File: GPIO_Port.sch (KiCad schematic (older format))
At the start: 73 parts, among them J6 Conn_02x20_Odd_Even

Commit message: Reroute ribbon connector protection circuitry, switch to single ribbon cable configuration.
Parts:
- added D2, D3, D4, D5: BAT54S, Package_TO_SOT_SMD:SOT-323_SC-70, symbol Diode:BAT54S
- added R1, R2, R3, R4: 50, Resistor_SMD:R_0603_1608Metric, symbol Device:R
- D1, D10, D11, D12, D13, D14, D15, D16, D17, D18, D19, D2, D20, D21, D22, D23, D24, D25, D26, D27, D28, D29, D3, D30, D31, D32, D33, D34, D35, D36, D4, D5, D6, D7, D8, D9: footprint Package_TO_SOT_SMD:SOT-23 -> Package_TO_SOT_SMD:SOT-323_SC-70
- R1, R10, R11, R12, R13, R14, R15, R16, R17, R18, R19, R2, R20, R21, R22, R23, R24, R25, R26, R27, R28, R29, R3, R30, R31, R32, R33, R34, R35, R36, R4, R5, R6, R7, R8, R9: footprint Resistor_SMD:R_0805_2012Metric -> Resistor_SMD:R_0603_1608Metric
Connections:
- net +5V is gone; now on net P11: J6.11 (Pin_11)
- net GP0 is gone; now on net GP1: R1.2
- net +3V3: now also D2.2, D3.2, D4.2, D5.2; no longer J6.29 (Pin_29)
- net GND: now also D2.1, D3.1, D4.1, D5.1; no longer J6.12 (Pin_12), J6.30 (Pin_30)
- net GP1: no longer R2.1
- net GP10: now also R10.1; no longer R11.2
- net GP11: now also R1.2; no longer R12.1
- net GP12: now also R3.1; no longer R13.2
- net GP13: now also R11.2; no longer R14.1
- net GP14: now also R12.1; no longer R15.2
- net GP15: now also R13.2; no longer R16.1
- net GP16: now also R14.1; no longer R17.2
- net GP17: now also R15.2; no longer R18.1
- net GP18: now also R16.1; no longer R19.2
- net GP19: now also R17.2; no longer R20.1
- net GP2: now also R2.1; no longer R3.2
- net GP20: now also R18.1; no longer R21.2
- net GP21: now also R19.2; no longer R22.1
- net GP22: now also R20.1; no longer R23.2
- net GP23: now also R21.2; no longer R24.1
- net GP24: now also R22.1; no longer R25.2
- net GP25: now also R23.2; no longer R26.1
- net GP26: now also R24.1; no longer R27.2
- net GP27: now also R25.2; no longer R28.1
- net GP28: now also R26.1; no longer R29.2
- net GP29: now also R2.2; no longer R30.1
- net GP3: now also R3.2; no longer R4.1
- net GP30: now also R4.1; no longer R31.2
- net GP31: now also R27.2; no longer R32.1
- net GP32: now also R28.1; no longer R33.2
- net GP33: now also R29.2; no longer R34.1
- net GP34: now also R30.1; no longer R35.2
- net GP35: now also R31.2; no longer R36.1
- net GP4: now also R4.1; no longer R5.2
- net GP5: now also R5.2; no longer R6.1
- net GP6: now also R6.1; no longer R7.2
- net GP7: now also R7.2; no longer R8.1
- net GP8: now also R8.1; no longer R9.2
- net GP9: now also R9.2; no longer R10.1
- net P1: now also J6.1 (Pin_1), R1.1; no longer J6.2 (Pin_2), R2.2
- net P10: now also J6.10 (Pin_10), R10.2; no longer J6.13 (Pin_13), R11.1
- net P11: now also R1.1; no longer J6.14 (Pin_14), R12.2
- net P12: now also J6.12 (Pin_12), R3.2; no longer J6.15 (Pin_15), R13.1
- net P13: now also J6.13 (Pin_13), R11.1; no longer J6.16 (Pin_16), R14.2
- net P14: now also J6.14 (Pin_14), R12.2; no longer J6.17 (Pin_17), R15.1
- net P15: now also J6.15 (Pin_15), R13.1; no longer J6.18 (Pin_18), R16.2
- net P16: now also J6.16 (Pin_16), R14.2; no longer J6.19 (Pin_19), R17.1
- net P17: now also J6.17 (Pin_17), R15.1; no longer J6.20 (Pin_20), R18.2
- net P18: now also J6.18 (Pin_18), R16.2; no longer J6.21 (Pin_21), R19.1
- net P19: now also J6.19 (Pin_19), R17.1; no longer J6.22 (Pin_22), R20.2
- net P2: now also J6.2 (Pin_2), R2.2; no longer J6.3 (Pin_3), R3.1
- net P20: now also J6.20 (Pin_20), R18.2; no longer J6.23 (Pin_23), R21.1
- net P21: now also J6.21 (Pin_21), R19.1; no longer J6.24 (Pin_24), R22.2
- net P22: now also J6.22 (Pin_22), R20.2; no longer J6.25 (Pin_25), R23.1
- net P23: now also J6.23 (Pin_23), R21.1; no longer J6.26 (Pin_26), R24.2
- net P24: now also J6.24 (Pin_24), R22.2; no longer J6.27 (Pin_27), R25.1
- net P25: now also J6.25 (Pin_25), R23.1; no longer J6.28 (Pin_28), R26.2
- net P26: now also J6.26 (Pin_26), R24.2; no longer J6.31 (Pin_31), R27.1
- net P27: now also J6.27 (Pin_27), R25.1; no longer J6.32 (Pin_32), R28.2
- net P28: now also J6.28 (Pin_28), R26.2; no longer J6.33 (Pin_33), R29.1
- net P29: now also J6.29 (Pin_29), R2.1; no longer J6.34 (Pin_34), R30.2
- net P3: now also J6.3 (Pin_3), R3.1; no longer J6.4 (Pin_4), R4.2
- net P30: now also J6.30 (Pin_30), R4.2; no longer J6.35 (Pin_35), R31.1
- net P31: now also J6.31 (Pin_31), R27.1; no longer J6.36 (Pin_36), R32.2
- net P32: now also J6.32 (Pin_32), R28.2; no longer J6.37 (Pin_37), R33.1
- net P33: now also J6.33 (Pin_33), R29.1; no longer J6.38 (Pin_38), R34.2
- net P34: now also J6.34 (Pin_34), R30.2; no longer J6.39 (Pin_39), R35.1
- net P35: now also J6.35 (Pin_35), R31.1; no longer J6.40 (Pin_40), R36.2
- net P4: now also J6.4 (Pin_4), R4.2; no longer J6.5 (Pin_5), R5.1
- net P5: now also J6.5 (Pin_5), R5.1; no longer J6.6 (Pin_6), R6.2
- net P6: now also J6.6 (Pin_6), R6.2; no longer J6.7 (Pin_7), R7.1
- net P7: now also J6.7 (Pin_7), R7.1; no longer J6.8 (Pin_8), R8.2
- net P8: now also J6.8 (Pin_8), R8.2; no longer J6.9 (Pin_9), R9.1
- net P9: now also J6.9 (Pin_9), R9.1; no longer J6.10 (Pin_10), R10.2
- removed net P0: D1.3, J6.1 (Pin_1), R1.1
- new net GP36: R32.1
- new net GP37: R33.2
- new net GP38: R34.1
- new net GP39: R35.2
- new net GP40: R36.1
- new net P36: D1.3, J6.36 (Pin_36), R32.2
- new net P37: D2.3, J6.37 (Pin_37), R33.1
- new net P38: D3.3, J6.38 (Pin_38), R34.2
- new net P39: D4.3, J6.39 (Pin_39), R35.1
- new net P40: D5.3, J6.40 (Pin_40), R36.2

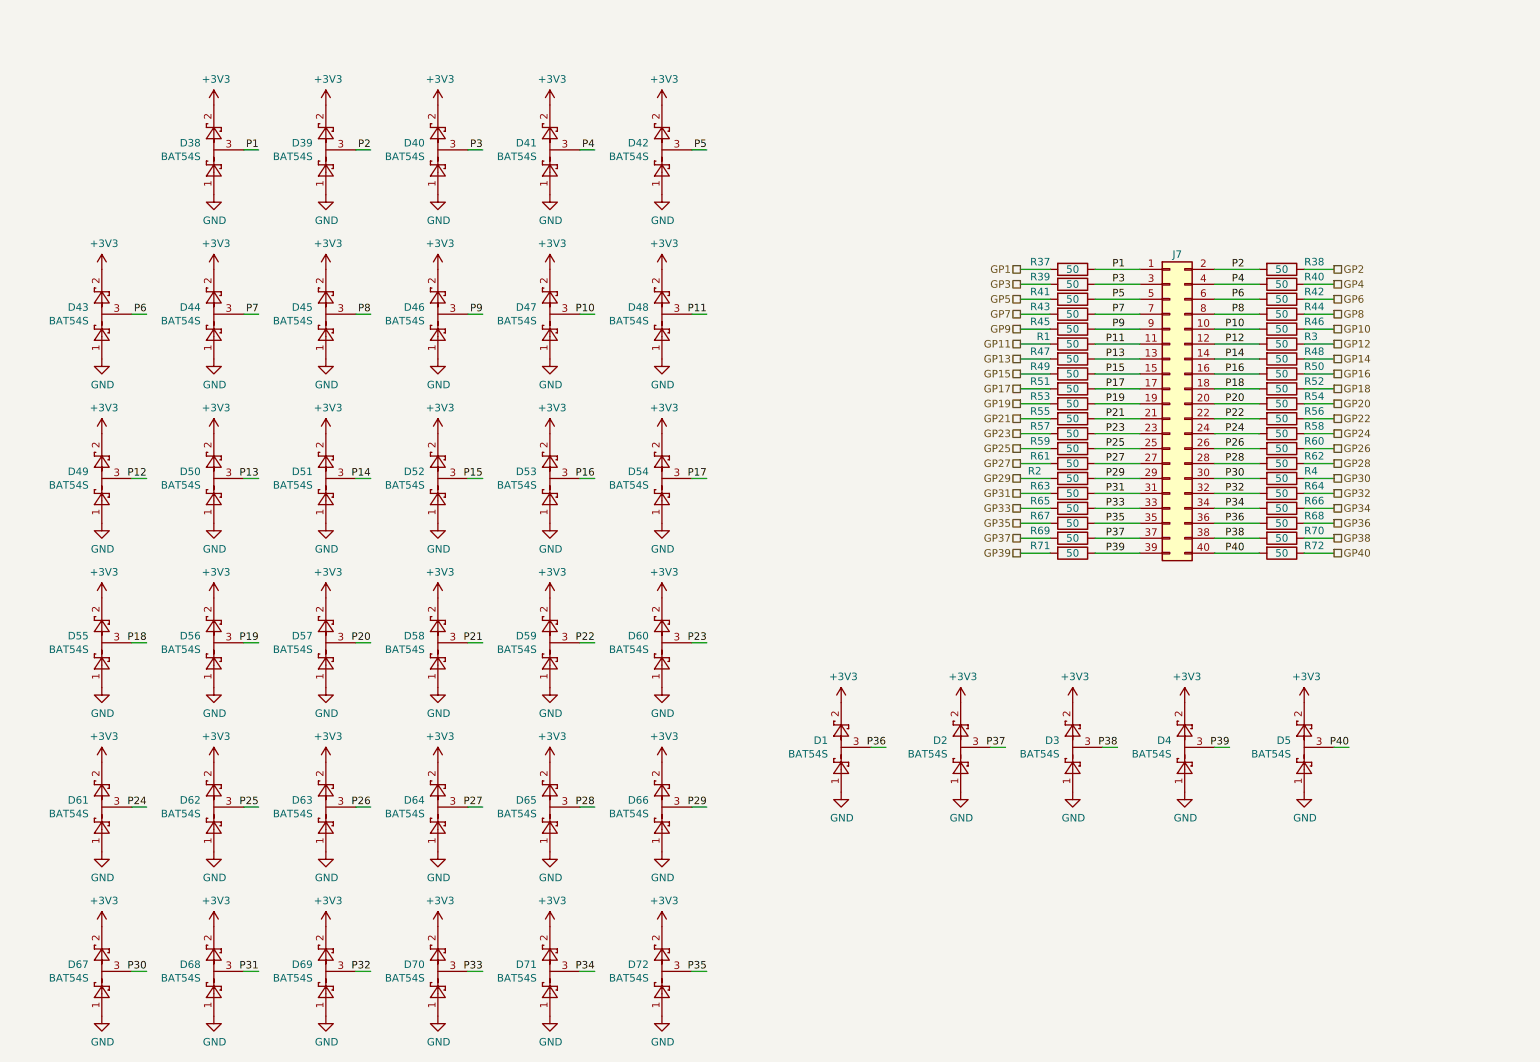
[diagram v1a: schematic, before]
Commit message: Change pin/bus labels in schematic
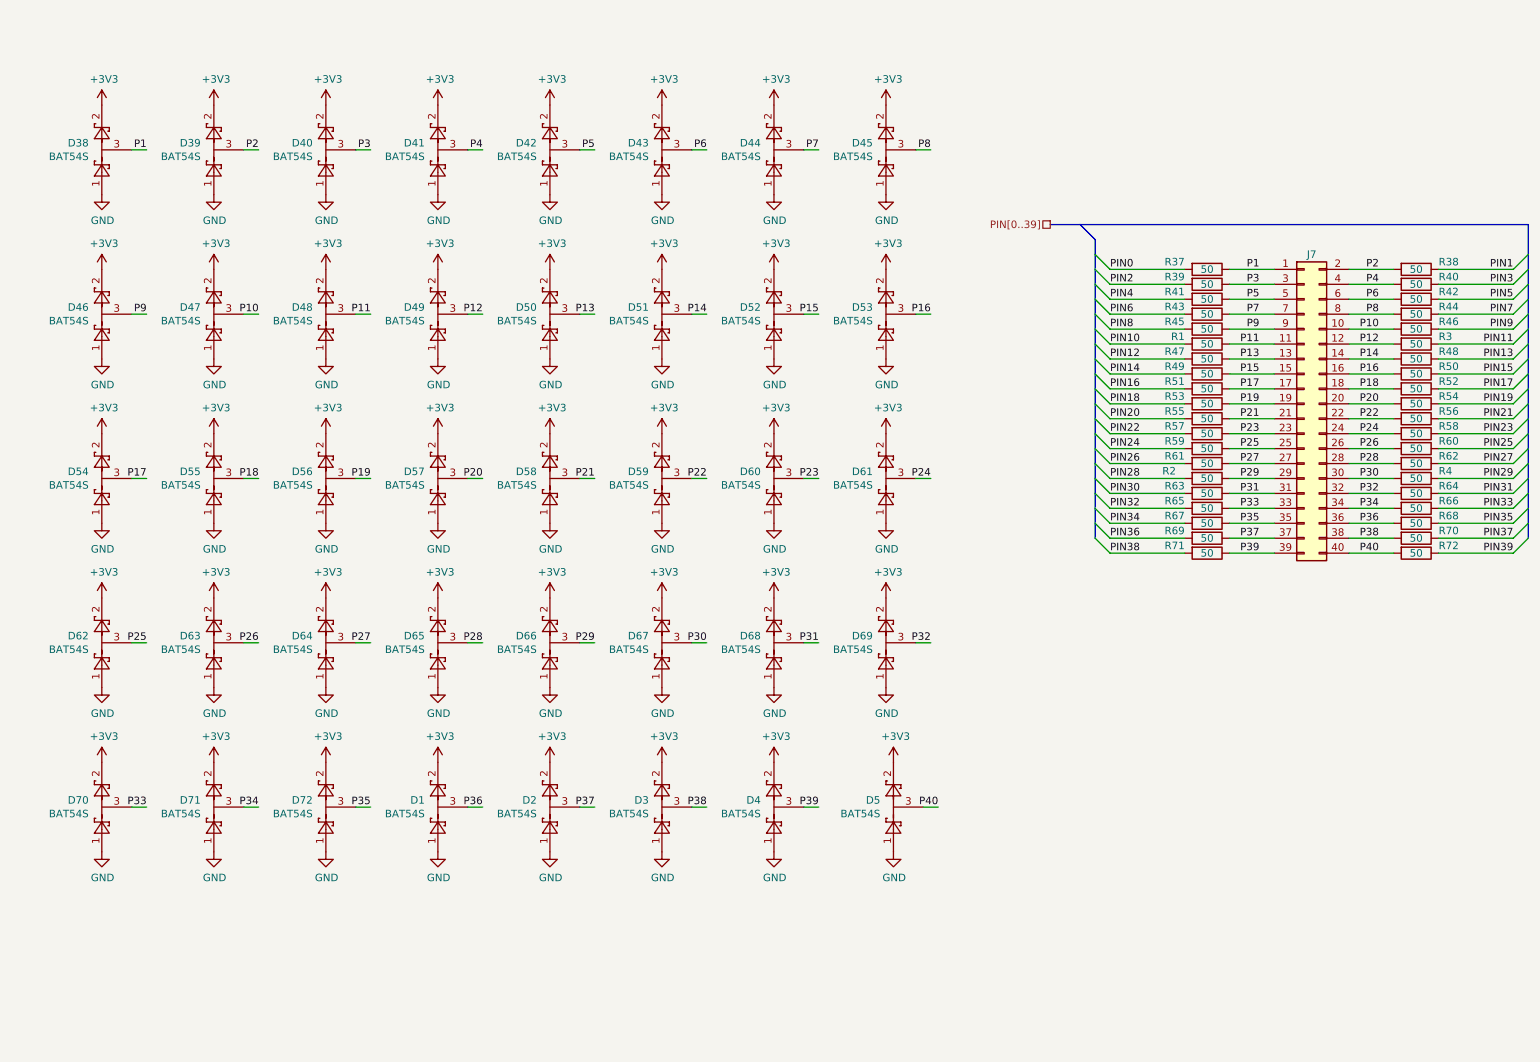
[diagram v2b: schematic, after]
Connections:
- net GP1 renamed PIN0
- net GP10 renamed PIN9
- net GP11 renamed PIN10
- net GP12 renamed PIN11
- net GP13 renamed PIN12
- net GP14 renamed PIN13
- net GP15 renamed PIN14
- net GP16 renamed PIN15
- net GP17 renamed PIN16
- net GP18 renamed PIN17
- net GP19 renamed PIN18
- net GP2 renamed PIN1
- net GP20 renamed PIN19
- net GP21 renamed PIN20
- net GP22 renamed PIN21
- net GP23 renamed PIN22
- net GP24 renamed PIN23
- net GP25 renamed PIN24
- net GP26 renamed PIN25
- net GP27 renamed PIN26
- net GP28 renamed PIN27
- net GP29 renamed PIN28
- net GP3 renamed PIN2
- net GP30 renamed PIN29
- net GP31 renamed PIN30
- net GP32 renamed PIN31
- net GP33 renamed PIN32
- net GP34 renamed PIN33
- net GP35 renamed PIN34
- net GP36 renamed PIN35
- net GP37 renamed PIN36
- net GP38 renamed PIN37
- net GP39 renamed PIN38
- net GP4 renamed PIN3
- net GP40 renamed PIN39
- net GP5 renamed PIN4
- net GP6 renamed PIN5
- net GP7 renamed PIN6
- net GP8 renamed PIN7
- net GP9 renamed PIN8
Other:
- moved on the sheet: D1, D2, D3, D38, D39, D4, D40, D41, D42, D43, D44, D45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

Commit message: Begin routing ribbon cable connector
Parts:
- renumbered D2 to D1, D11 to D10, D12 to D11, D13 to D12, D14 to D13, D15 to D14, D16 to D15, D17 to D16, D18 to D17, D19 to D18, D20 to D19, D3 to D2, D21 to D20, D22 to D21, D23 to D22, D24 to D23, D25 to D24, D26 to D25, D27 to D26, D28 to D27, D29 to D28, D30 to D29, D4 to D3, D31 to D30, D32 to D31, D33 to D32, D34 to D33, D35 to D34, D36 to D35, D1 to D36, D2 to D37, D3 to D38, D4 to D39, D5 to D4, D5 to D40, D6 to D5, D7 to D6, D8 to D7, D9 to D8, D10 to D9, J6 to J5, R1 to R11, R3 to R12, R11 to R13, R12 to R14, R13 to R15, R14 to R16, R15 to R17, R16 to R18, R17 to R19, R18 to R20, R19 to R21, R20 to R22, R21 to R23, R22 to R24, R23 to R25, R24 to R26, R25 to R27, R26 to R28, R2 to R29, R4 to R30, R27 to R31, R28 to R32, R29 to R33, R30 to R34, R31 to R35, R32 to R36, R33 to R37, R34 to R38, R35 to R39, R36 to R40

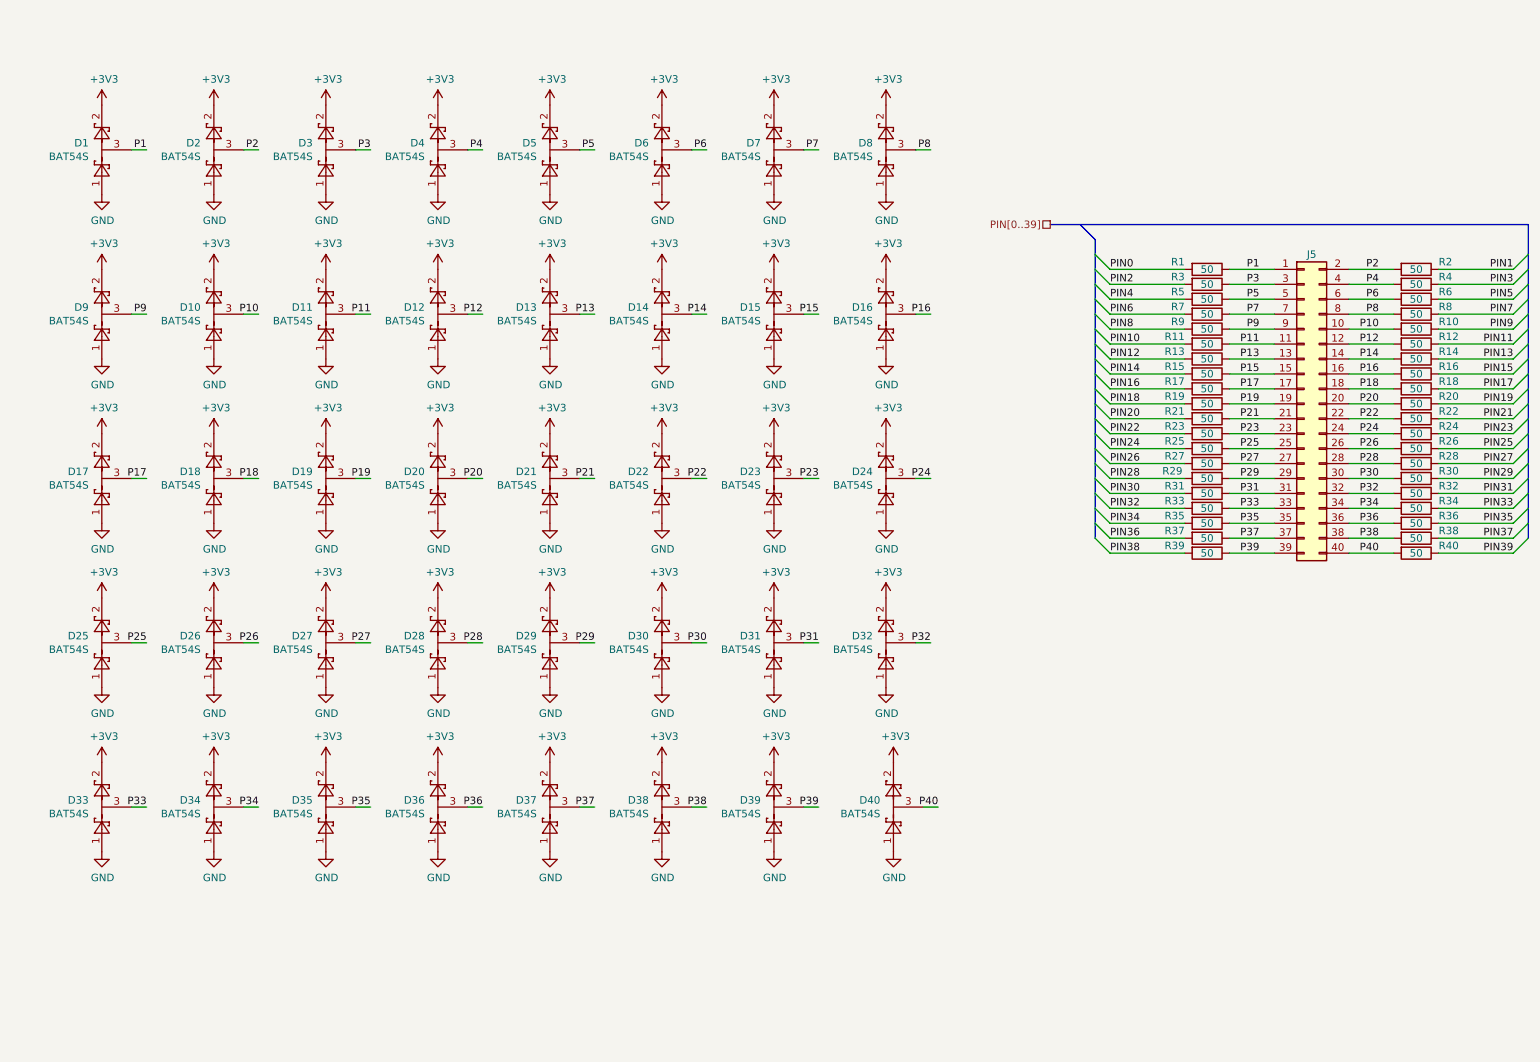
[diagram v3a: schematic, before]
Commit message: Finish routing GPIO port
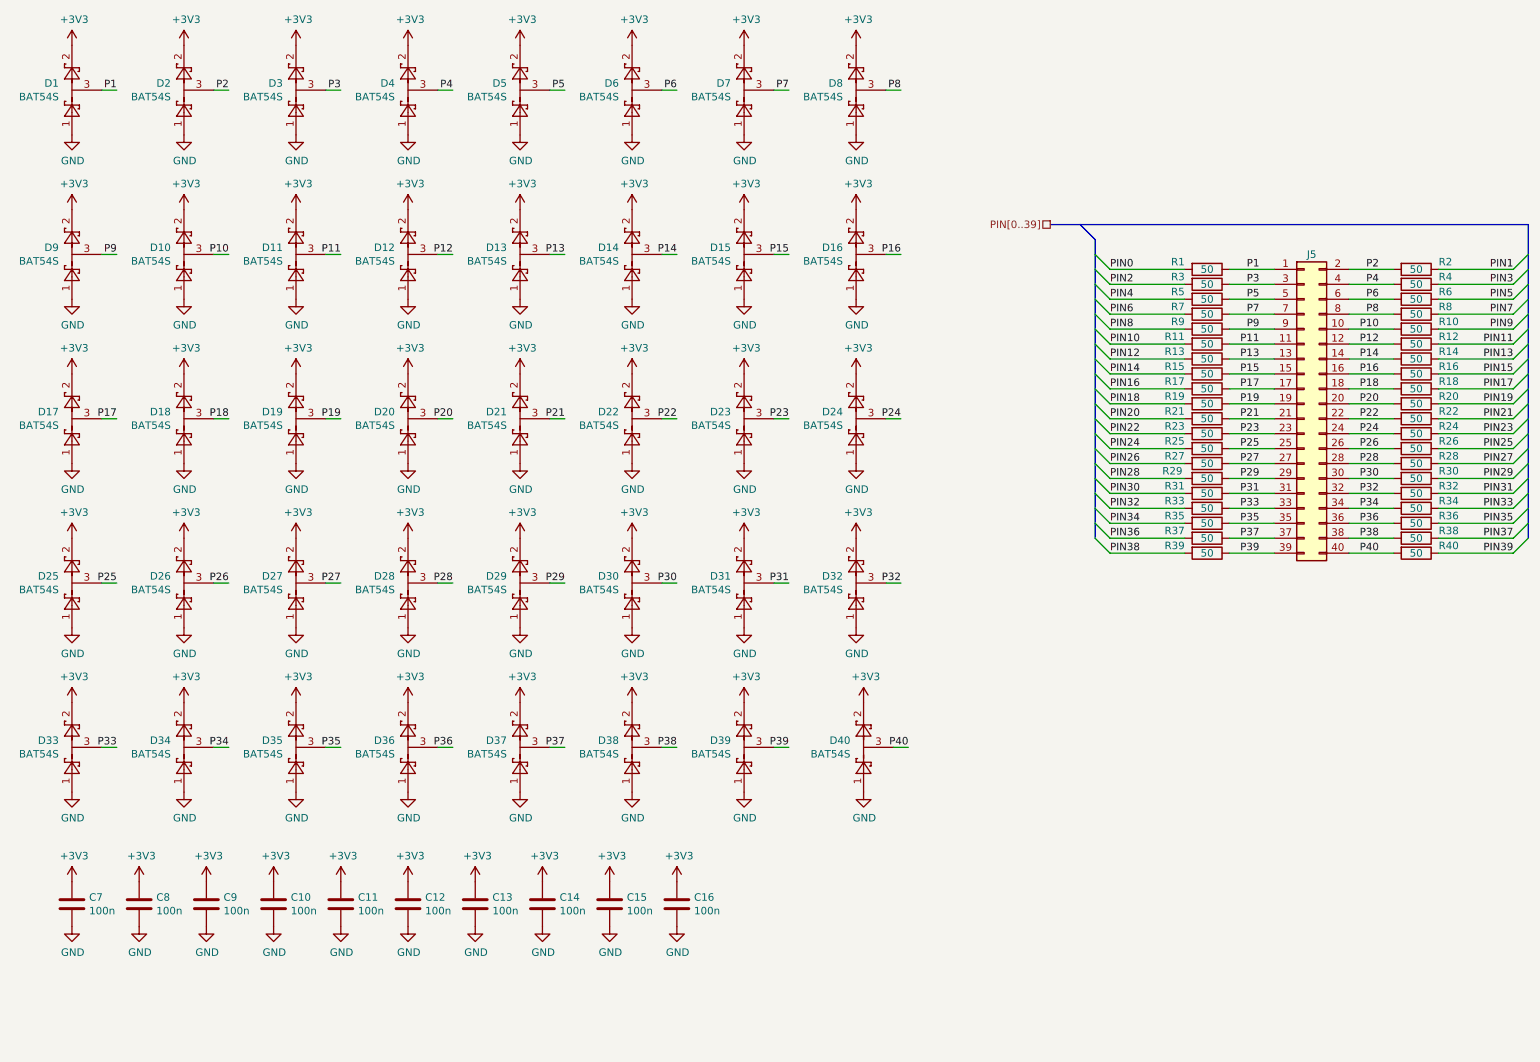
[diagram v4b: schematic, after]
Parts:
- added C10, C11, C12, C13, C14, C15, C16, C7, C8, C9: 100n, Capacitor_SMD:C_0805_2012Metric, symbol Device:C
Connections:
- net +3V3: now also C10.1, C11.1, C12.1, C13.1, C14.1, C15.1, C16.1, C7.1, C8.1, C9.1
- net GND: now also C10.2, C11.2, C12.2, C13.2, C14.2, C15.2, C16.2, C7.2, C8.2, C9.2
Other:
- moved on the sheet: D1, D10, D11, D12, D13, D14, D15, D16, D17, D18, D19, D2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

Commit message: Change BAT54S diode packages back to to SOT-23
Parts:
- D1, D10, D11, D12, D13, D14, D15, D16, D17, D18, D19, D2, D20, D21, D22, D23, D24, D25, D26, D27, D28, D29, D3, D30, D31, D32, D33, D34, D35, D36, D37, D38, D39, D4, D40, D5, D6, D7, D8, D9: footprint Package_TO_SOT_SMD:SOT-323_SC-70 -> Package_TO_SOT_SMD:SOT-23
